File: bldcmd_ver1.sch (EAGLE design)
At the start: 94 parts, among them CN1 DF61-2P-2.2V(23), CN2 DF65-3P-1.7V(21), IC1 STSPIN32F0A, IC2 AS5047P-ATSM, IC3 ADM4852ACPZ-REEL7, Q1 PSMN2R4-30MLD, Q2 PSMN2R4-30MLD, Q3 PSMN2R4-30MLD, Q4 PSMN2R4-30MLD, Q5 PSMN2R4-30MLD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

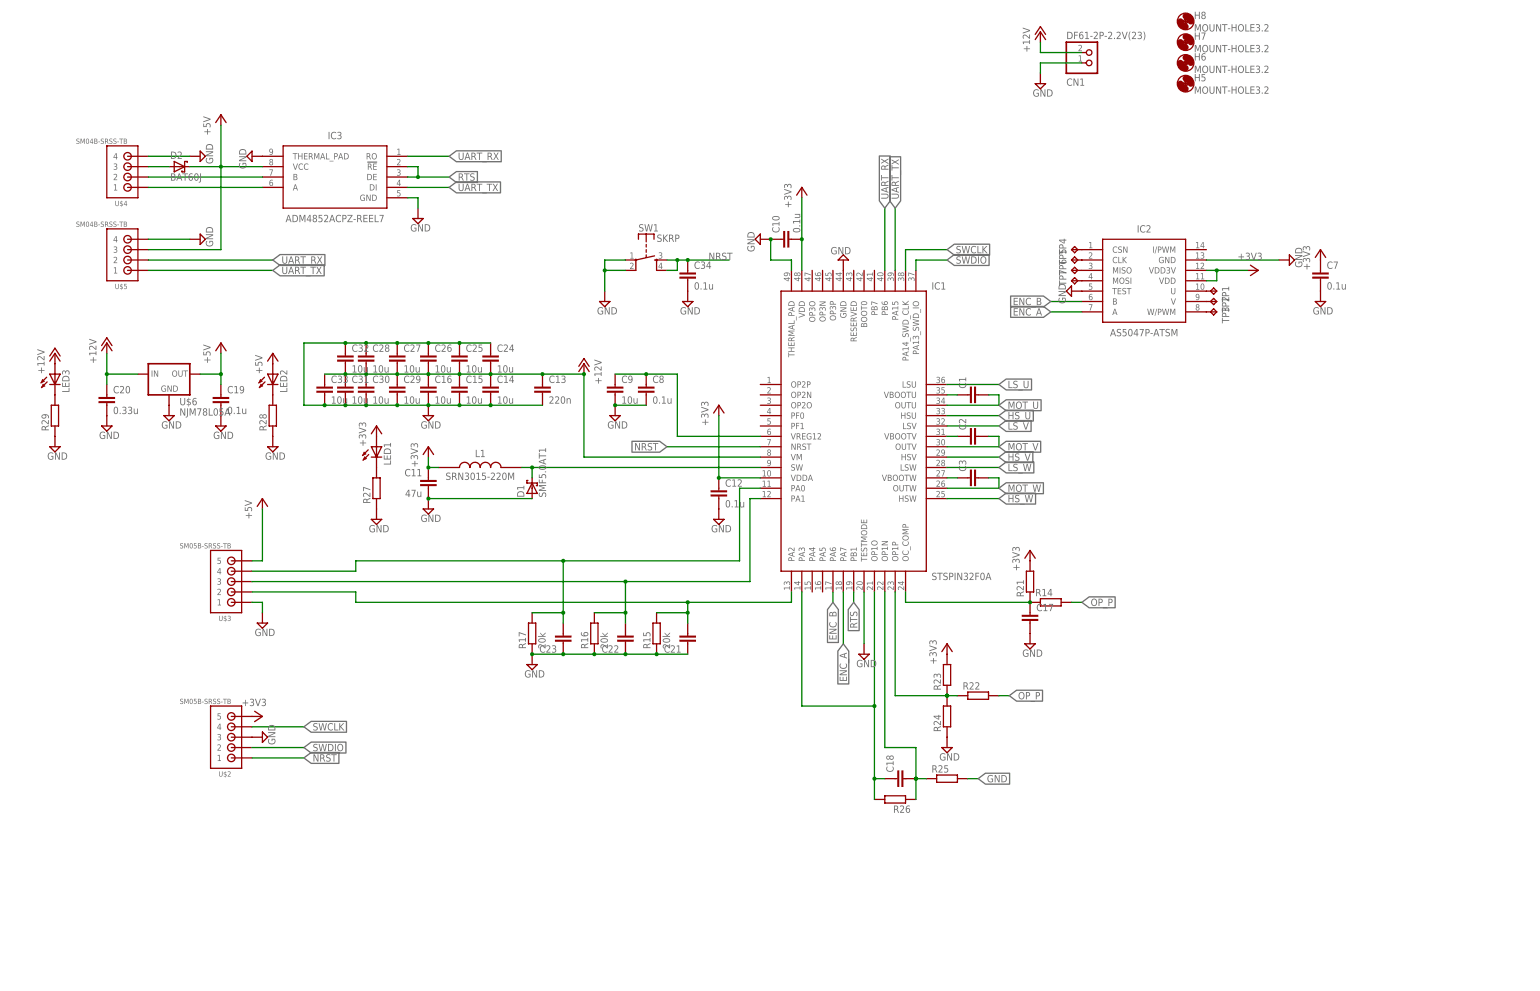
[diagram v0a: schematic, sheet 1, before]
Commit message: #3 の対応，エンコーダ入力からSPI接続に変更
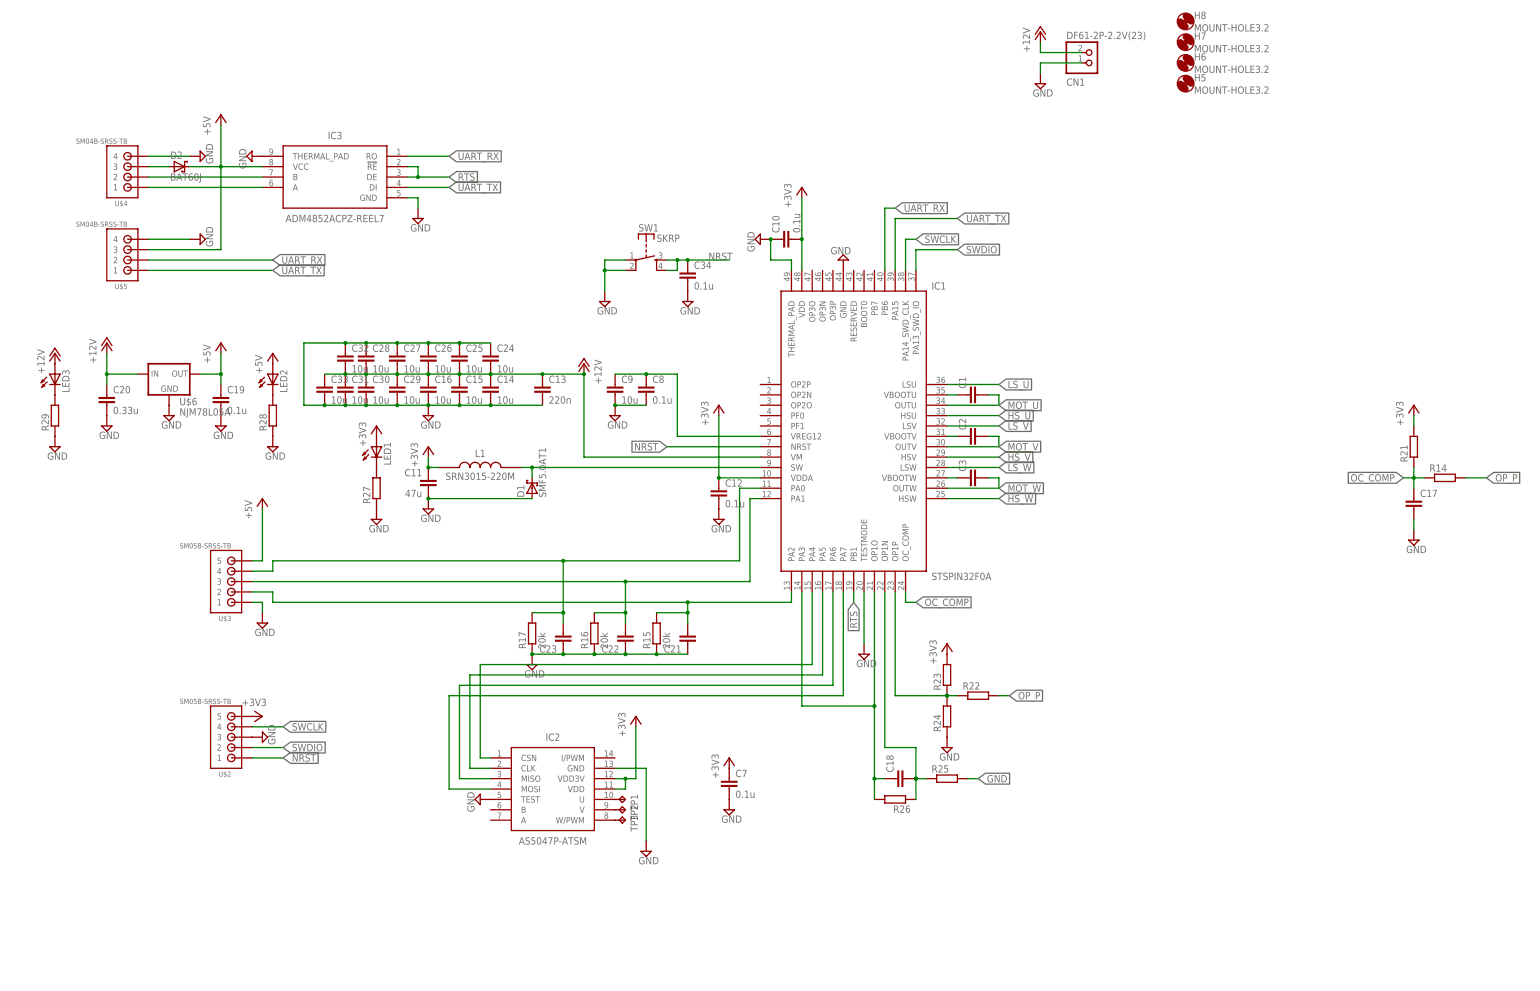
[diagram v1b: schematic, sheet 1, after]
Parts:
- removed TP4, TP5, TP6, TP7: TPTP08R, testpad:TPTP08R
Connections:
- net N$10 renamed OC_COMP
- removed net ENC_A: IC1.PA7, IC2.A
- removed net ENC_B: IC1.PA6, IC2.B
- net N$12: now also IC1.PA6; no longer TP6.TP
- net N$17: now also IC1.PA7; no longer TP7.TP
- net N$7: now also IC1.PA4; no longer TP4.TP
- net N$8: now also IC1.PA5; no longer TP5.TP
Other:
- moved on the sheet: C17, C7, IC2, R14, R21, TP1, TP2, TP3

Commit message: 修正したSHコネクタの変更を適用
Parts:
- removed U$2, U$3: SM05B-SRSS-TB, JST-SH:SM05B-SRSS-TB
- removed U$4, U$5: SM04B-SRSS-TB, JST-SH:SM04B-SRSS-TB
- added CN3, CN4: SM04B-SRSS-TB, scramble-con-jst:SM04B-SRSS-TB
- added CN5, CN6: SM05B-SRSS-TB, scramble-con-jst:SM05B-SRSS-TB
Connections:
- net +3V3: now also CN6.5; no longer U$2.5
- net +5V: now also CN4.3, CN5.5; no longer U$3.5, U$5.3
- net GND: now also CN3.4, CN4.4, CN5.1, CN6.3; no longer U$2.3, U$3.1, U$4.4, U$5.4
- net N$23: now also CN5.2; no longer U$3.2
- net N$24: now also CN5.3; no longer U$3.3
- net N$25: now also CN5.4; no longer U$3.4
- net N$29: now also CN3.2; no longer U$4.2
- net N$30: now also CN3.3; no longer U$4.3
- net N$32: now also CN3.1; no longer U$4.1
- net NRST: now also CN6.1; no longer U$2.1
- net SWCLK: now also CN6.4; no longer U$2.4
- net SWDIO: now also CN6.2; no longer U$2.2
- net UART_RX: now also CN4.2; no longer U$5.2
- net UART_TX: now also CN4.1; no longer U$5.1
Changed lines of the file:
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@@
 <?xml version="1.0" encoding="utf-8"?>
 <!DOCTYPE eagle SYSTEM "eagle.dtd">
-<eagle version="8.4.0">
+<eagle version="8.3.2">
 <drawing>
 <settings>
@@
 <setting verticaltext="up"/>
 </settings>
-<grid distance="0.1" unitdist="inch" unit="inch" style="lines" multiple="1" display="no" altdistance="0.05" altunitdist="inch" altunit="inch"/>
+<grid distance="0.1" unitdist="inch" unit="inch" style="lines" multiple="1" display="no" altdistance="0.01" altunitdist="inch" altunit="inch"/>
 <layers>
 <layer number="1" name="Top" color="4" fill="1" visible="no" active="no"/>
@@
 <part name="SUPPLY21" library="supply2" library_urn="urn:adsk.eagle:library:372" deviceset="GND" device=""/>
 <part name="+3V8" library="supply1" library_urn="urn:adsk.eagle:library:371" deviceset="+3V3" device=""/>
-<part name="U$2" library="JST-SH" deviceset="SM05B-SRSS-TB" device=""/>
-<part name="U$3" library="JST-SH" deviceset="SM05B-SRSS-TB" device=""/>
-<part name="U$4" library="JST-SH" deviceset="SM04B-SRSS-TB" device=""/>
-<part name="U$5" library="JST-SH" deviceset="SM04B-SRSS-TB" device=""/>
 <part name="P+4" library="supply1" library_urn="urn:adsk.eagle:library:371" deviceset="+12V" device=""/>
 <part name="SUPPLY22" library="supply2" library_urn="urn:adsk.eagle:library:372" deviceset="GND" device=""/>
@@
 <part name="CN1" library="scramble-con-hirose" deviceset="DF61-2P-2.2V(23)" device=""/>
 <part name="CN2" library="scramble-con-hirose" deviceset="DF65-3P-1.7V(21)" device=""/>
+<part name="CN3" library="scramble-con-jst" deviceset="?M04B-SRSS-TB" device="S"/>
+<part name="CN4" library="scramble-con-jst" deviceset="?M04B-SRSS-TB" device="S"/>
+<part name="CN5" library="scramble-con-jst" deviceset="?M05B-SRSS-TB" device="S"/>
+<part name="CN6" library="scramble-con-jst" deviceset="?M05B-SRSS-TB" device="S"/>
 </parts>
 <sheets>
@@
 <instance part="SUPPLY21" gate="GND" x="-114.3" y="-86.36" rot="R90"/>
 <instance part="+3V8" gate="G$1" x="-114.3" y="-81.28" rot="R270"/>
-<instance part="U$2" gate="G$2" x="-121.92" y="-86.36" rot="R180"/>
-<instance part="U$3" gate="G$2" x="-121.92" y="-48.26" rot="R180"/>
-<instance part="U$4" gate="G$1" x="-147.32" y="53.34" rot="R180"/>
-<instance part="U$5" gate="G$1" x="-147.32" y="33.02" rot="R180"/>
 <instance part="P+4" gate="1" x="-152.4" y="10.16"/>
 <instance part="SUPPLY22" gate="GND" x="-137.16" y="-7.62"/>
@@
 <instance part="H8" gate="G$1" x="111.76" y="88.9"/>
 <instance part="CN1" gate="G$1" x="86.36" y="78.74" rot="MR180"/>
+<instance part="CN3" gate="G$1" x="-147.32" y="50.8" rot="R180"/>
+<instance part="CN4" gate="G$1" x="-147.32" y="30.48" rot="R180"/>
+<instance part="CN5" gate="G$1" x="-116.84" y="-48.26" rot="R180"/>
+<instance part="CN6" gate="G$1" x="-116.84" y="-86.36" rot="R180"/>
 </instances>
 <busses>
@@
 <pinref part="SUPPLY20" gate="GND" pin="GND"/>
 <wire x1="-114.3" y1="-53.34" x2="-114.3" y2="-55.88" width="0.1524" layer="91"/>
-<pinref part="U$3" gate="G$2" pin="1"/>
-</segment>
-<segment>
-<pinref part="SUPPLY21" gate="GND" pin="GND"/>
-<pinref part="U$2" gate="G$2" pin="3"/>
+<pinref part="CN5" gate="G$1" pin="1"/>
 </segment>
 <segment>
 <pinref part="SUPPLY19" gate="GND" pin="GND"/>
-<pinref part="U$4" gate="G$1" pin="4"/>
-<wire x1="-142.24" y1="55.88" x2="-132.08" y2="55.88" width="0.1524" layer="91"/>
+<wire x1="-147.32" y1="55.88" x2="-132.08" y2="55.88" width="0.1524" layer="91"/>
+<pinref part="CN3" gate="G$1" pin="4"/>
 </segment>
 <segment>
 <pinref part="SUPPLY18" gate="GND" pin="GND"/>
-<pinref part="U$5" gate="G$1" pin="4"/>
-<wire x1="-142.24" y1="35.56" x2="-132.08" y2="35.56" width="0.1524" layer="91"/>
+<wire x1="-147.32" y1="35.56" x2="-132.08" y2="35.56" width="0.1524" layer="91"/>
+<pinref part="CN4" gate="G$1" pin="4"/>
 </segment>
 <segment>
@@
 <wire x1="76.2" y1="78.74" x2="86.36" y2="78.74" width="0.1524" layer="91"/>
 </segment>
+<segment>
+<pinref part="SUPPLY21" gate="GND" pin="GND"/>
+<pinref part="CN6" gate="G$1" pin="3"/>
+</segment>
 </net>
 <net name="+3V3" class="0">
@@
 </segment>
 <segment>
-<pinref part="+3V8" gate="G$1" pin="+3V3"/>
-<pinref part="U$2" gate="G$2" pin="5"/>
-</segment>
-<segment>
 <pinref part="+3V9" gate="G$1" pin="+3V3"/>
 <pinref part="LED1" gate="G$1" pin="A"/>
+</segment>
+<segment>
+<pinref part="+3V8" gate="G$1" pin="+3V3"/>
+<pinref part="CN6" gate="G$1" pin="5"/>
 </segment>
 </net>
@@
 </segment>
 <segment>
-<wire x1="-142.24" y1="27.94" x2="-111.76" y2="27.94" width="0.1524" layer="91"/>
+<wire x1="-147.32" y1="27.94" x2="-111.76" y2="27.94" width="0.1524" layer="91"/>
 <label x="-111.76" y="27.94" size="1.778" layer="95" xref="yes"/>
-<pinref part="U$5" gate="G$1" pin="1"/>
+<pinref part="CN4" gate="G$1" pin="1"/>
 </segment>
 </net>
@@
 </segment>
 <segment>
-<wire x1="-142.24" y1="30.48" x2="-111.76" y2="30.48" width="0.1524" layer="91"/>
+<wire x1="-147.32" y1="30.48" x2="-111.76" y2="30.48" width="0.1524" layer="91"/>
 <label x="-111.76" y="30.48" size="1.778" layer="95" xref="yes"/>
-<pinref part="U$5" gate="G$1" pin="2"/>
+<pinref part="CN4" gate="G$1" pin="2"/>
 </segment>
 </net>
@@
 <wire x1="-116.84" y1="-50.8" x2="-111.76" y2="-50.8" width="0.1524" layer="91"/>
 <wire x1="-111.76" y1="-50.8" x2="-111.76" y2="-53.34" width="0.1524" layer="91"/>
-<pinref part="U$3" gate="G$2" pin="2"/>
 <pinref part="IC1" gate="G$1" pin="PA2"/>
 <wire x1="-111.76" y1="-53.34" x2="-10.16" y2="-53.34" width="0.1524" layer="91"/>
@@
 <junction x="-10.16" y="-53.34"/>
 <junction x="-10.16" y="-55.88"/>
+<pinref part="CN5" gate="G$1" pin="2"/>
 </segment>
 </net>
 <net name="N$24" class="0">
 <segment>
-<pinref part="U$3" gate="G$2" pin="3"/>
 <pinref part="IC1" gate="G$1" pin="PA1"/>
 <wire x1="7.62" y1="-27.94" x2="5.08" y2="-27.94" width="0.1524" layer="91"/>
@@
 <wire x1="-33.02" y1="-55.88" x2="-25.4" y2="-55.88" width="0.1524" layer="91"/>
 <junction x="-25.4" y="-55.88"/>
+<pinref part="CN5" gate="G$1" pin="3"/>
 </segment>
 </net>
@@
 <wire x1="-116.84" y1="-45.72" x2="-111.76" y2="-45.72" width="0.1524" layer="91"/>
 <wire x1="-111.76" y1="-45.72" x2="-111.76" y2="-43.18" width="0.1524" layer="91"/>
-<pinref part="U$3" gate="G$2" pin="4"/>
 <pinref part="IC1" gate="G$1" pin="PA0"/>
 <wire x1="7.62" y1="-25.4" x2="2.54" y2="-25.4" width="0.1524" layer="91"/>
@@
 <wire x1="-48.26" y1="-55.88" x2="-40.64" y2="-55.88" width="0.1524" layer="91"/>
 <junction x="-40.64" y="-55.88"/>
+<pinref part="CN5" gate="G$1" pin="4"/>
 </segment>
 </net>
@@
 <wire x1="-116.84" y1="-91.44" x2="-109.22" y2="-91.44" width="0.1524" layer="91"/>
 <label x="-109.22" y="-91.44" size="1.778" layer="95" xref="yes"/>
-<pinref part="U$2" gate="G$2" pin="1"/>
+<pinref part="CN6" gate="G$1" pin="1"/>
 </segment>
 <segment>
@@
 <wire x1="-116.84" y1="-88.9" x2="-109.22" y2="-88.9" width="0.1524" layer="91"/>
 <label x="-109.22" y="-88.9" size="1.778" layer="95" xref="yes"/>
-<pinref part="U$2" gate="G$2" pin="2"/>
+<pinref part="CN6" gate="G$1" pin="2"/>
 </segment>
 </net>
@@
 <wire x1="-116.84" y1="-83.82" x2="-109.22" y2="-83.82" width="0.1524" layer="91"/>
 <label x="-109.22" y="-83.82" size="1.778" layer="95" xref="yes"/>
-<pinref part="U$2" gate="G$2" pin="4"/>
+<pinref part="CN6" gate="G$1" pin="4"/>
 </segment>
 </net>
@@
 <segment>
 <pinref part="IC3" gate="G$1" pin="B"/>
-<wire x1="-114.3" y1="50.8" x2="-142.24" y2="50.8" width="0.1524" layer="91"/>
-<pinref part="U$4" gate="G$1" pin="2"/>
+<wire x1="-114.3" y1="50.8" x2="-147.32" y2="50.8" width="0.1524" layer="91"/>
+<pinref part="CN3" gate="G$1" pin="2"/>
 </segment>
 </net>
@@
 <segment>
 <pinref part="IC3" gate="G$1" pin="A"/>
-<wire x1="-114.3" y1="48.26" x2="-142.24" y2="48.26" width="0.1524" layer="91"/>
-<pinref part="U$4" gate="G$1" pin="1"/>
+<wire x1="-114.3" y1="48.26" x2="-147.32" y2="48.26" width="0.1524" layer="91"/>
+<pinref part="CN3" gate="G$1" pin="1"/>
 </segment>
 </net>
@@
 <wire x1="-116.84" y1="-43.18" x2="-114.3" y2="-43.18" width="0.1524" layer="91"/>
 <wire x1="-114.3" y1="-43.18" x2="-114.3" y2="-30.48" width="0.1524" layer="91"/>
-<pinref part="U$3" gate="G$2" pin="5"/>
 <pinref part="P+5" gate="1" pin="+5V"/>
+<pinref part="CN5" gate="G$1" pin="5"/>
 </segment>
 <segment>
@@
 <wire x1="-124.46" y1="53.34" x2="-124.46" y2="63.5" width="0.1524" layer="91"/>
 <junction x="-124.46" y="53.34"/>
-<wire x1="-142.24" y1="33.02" x2="-124.46" y2="33.02" width="0.1524" layer="91"/>
+<wire x1="-147.32" y1="33.02" x2="-124.46" y2="33.02" width="0.1524" layer="91"/>
 <wire x1="-124.46" y1="33.02" x2="-124.46" y2="53.34" width="0.1524" layer="91"/>
-<pinref part="U$5" gate="G$1" pin="3"/>
 <pinref part="P+6" gate="1" pin="+5V"/>
 <pinref part="D2" gate="G$1" pin="C"/>
 <wire x1="-132.08" y1="53.34" x2="-124.46" y2="53.34" width="0.1524" layer="91"/>
+<pinref part="CN4" gate="G$1" pin="3"/>
 </segment>
 <segment>
@@
 <net name="N$30" class="0">
 <segment>
-<pinref part="U$4" gate="G$1" pin="3"/>
-<wire x1="-142.24" y1="53.34" x2="-137.16" y2="53.34" width="0.1524" layer="91"/>
+<wire x1="-147.32" y1="53.34" x2="-137.16" y2="53.34" width="0.1524" layer="91"/>
 <pinref part="D2" gate="G$1" pin="A"/>
-</segment>
-</net>
+<pinref part="CN3" gate="G$1" pin="3"/>
+</segment>
+</net>

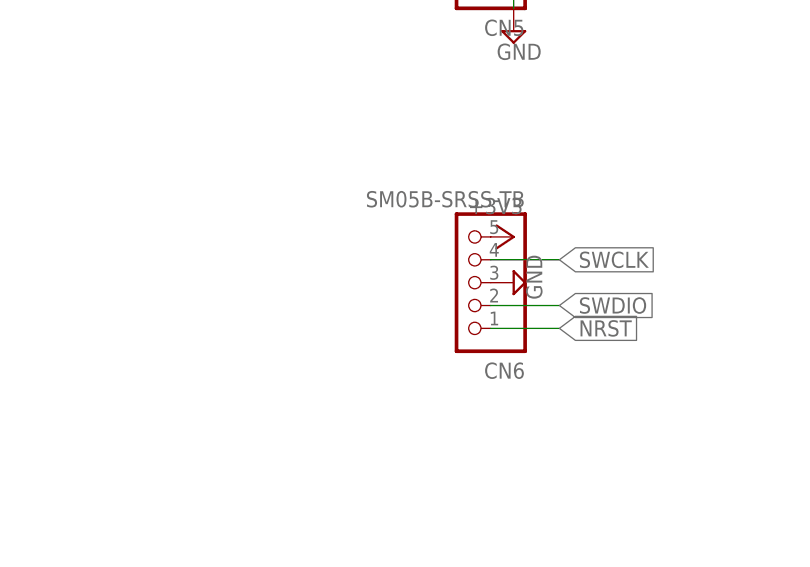
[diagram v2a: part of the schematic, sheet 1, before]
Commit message: ST-Linkのコネクタの接続順を入れ替えた
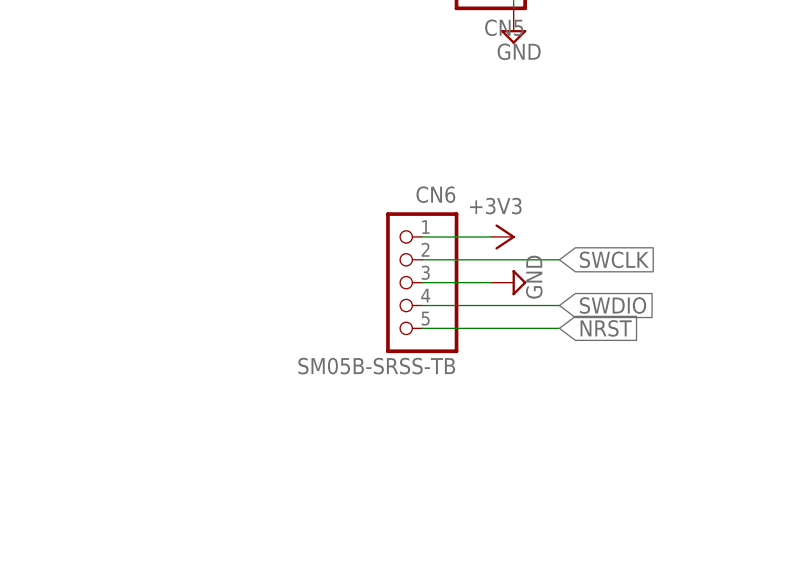
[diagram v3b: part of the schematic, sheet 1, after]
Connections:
- net +3V3: now also CN6.1; no longer CN6.5
- net NRST: now also CN6.5; no longer CN6.1
- net SWCLK: now also CN6.2; no longer CN6.4
- net SWDIO: now also CN6.4; no longer CN6.2
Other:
- moved on the sheet: CN6
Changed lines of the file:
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@@
 <instance part="CN4" gate="G$1" x="-147.32" y="30.48" rot="R180"/>
 <instance part="CN5" gate="G$1" x="-116.84" y="-48.26" rot="R180"/>
-<instance part="CN6" gate="G$1" x="-116.84" y="-86.36" rot="R180"/>
+<instance part="CN6" gate="G$1" x="-124.46" y="-86.36" rot="MR0"/>
 </instances>
 <busses>
@@
 <segment>
 <pinref part="SUPPLY21" gate="GND" pin="GND"/>
+<wire x1="-124.46" y1="-86.36" x2="-116.84" y2="-86.36" width="0.1524" layer="91"/>
 <pinref part="CN6" gate="G$1" pin="3"/>
 </segment>
@@
 <segment>
 <pinref part="+3V8" gate="G$1" pin="+3V3"/>
-<pinref part="CN6" gate="G$1" pin="5"/>
+<wire x1="-124.46" y1="-81.28" x2="-116.84" y2="-81.28" width="0.1524" layer="91"/>
+<pinref part="CN6" gate="G$1" pin="1"/>
 </segment>
 </net>
@@
 </segment>
 <segment>
-<wire x1="-116.84" y1="-91.44" x2="-109.22" y2="-91.44" width="0.1524" layer="91"/>
+<wire x1="-124.46" y1="-91.44" x2="-109.22" y2="-91.44" width="0.1524" layer="91"/>
 <label x="-109.22" y="-91.44" size="1.778" layer="95" xref="yes"/>
-<pinref part="CN6" gate="G$1" pin="1"/>
+<pinref part="CN6" gate="G$1" pin="5"/>
 </segment>
 <segment>
@@
 </segment>
 <segment>
-<wire x1="-116.84" y1="-88.9" x2="-109.22" y2="-88.9" width="0.1524" layer="91"/>
+<wire x1="-124.46" y1="-88.9" x2="-109.22" y2="-88.9" width="0.1524" layer="91"/>
 <label x="-109.22" y="-88.9" size="1.778" layer="95" xref="yes"/>
-<pinref part="CN6" gate="G$1" pin="2"/>
+<pinref part="CN6" gate="G$1" pin="4"/>
 </segment>
 </net>
@@
 </segment>
 <segment>
-<wire x1="-116.84" y1="-83.82" x2="-109.22" y2="-83.82" width="0.1524" layer="91"/>
+<wire x1="-124.46" y1="-83.82" x2="-109.22" y2="-83.82" width="0.1524" layer="91"/>
 <label x="-109.22" y="-83.82" size="1.778" layer="95" xref="yes"/>
-<pinref part="CN6" gate="G$1" pin="4"/>
-</segment>
-</net>
+<pinref part="CN6" gate="G$1" pin="2"/>
+</segment>
+</net>
